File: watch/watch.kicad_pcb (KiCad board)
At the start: 2 copper layers, 36 x 36 mm, 102 parts, among them IC1 IS32FL3237-TQLA3-TR, SW1 ButtonWakeup, U1 STM32L031F4Px, Y1 CR_32kHz

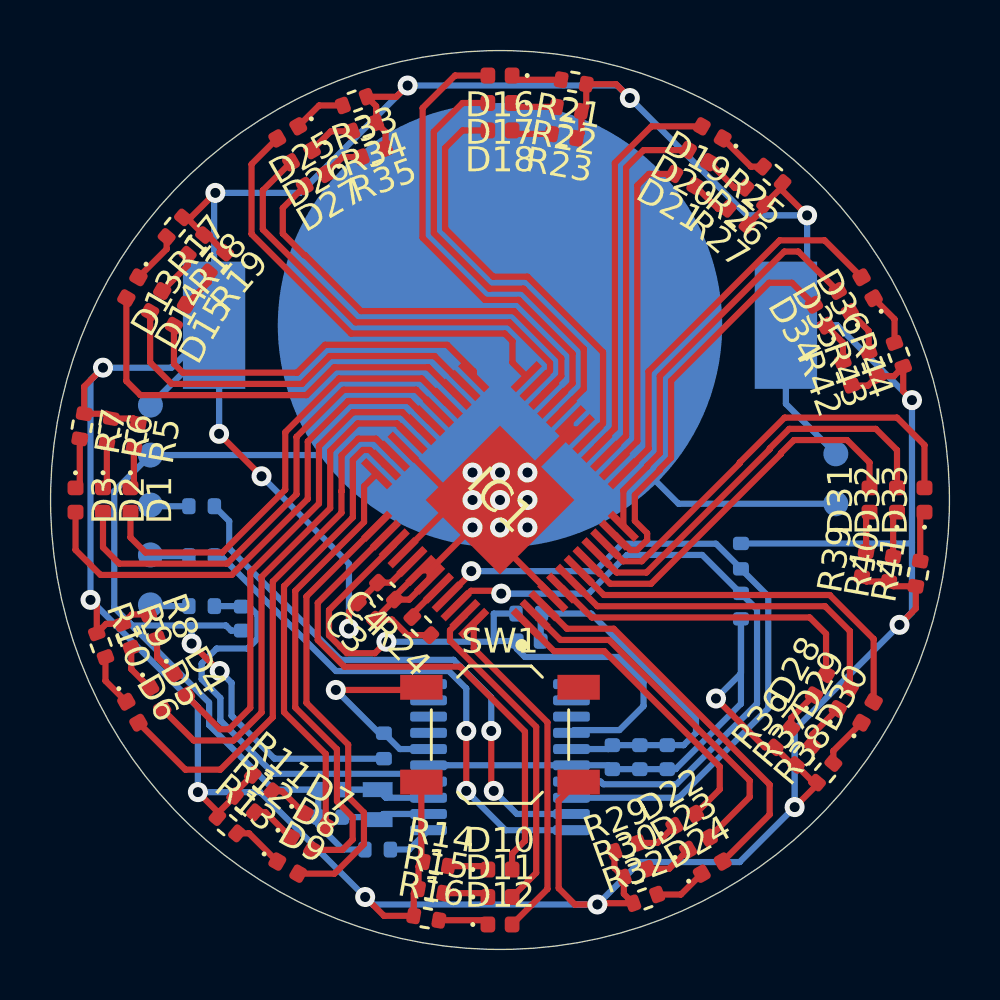
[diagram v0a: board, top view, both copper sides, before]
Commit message: no more vias below metallic components; cleaned up some tracks
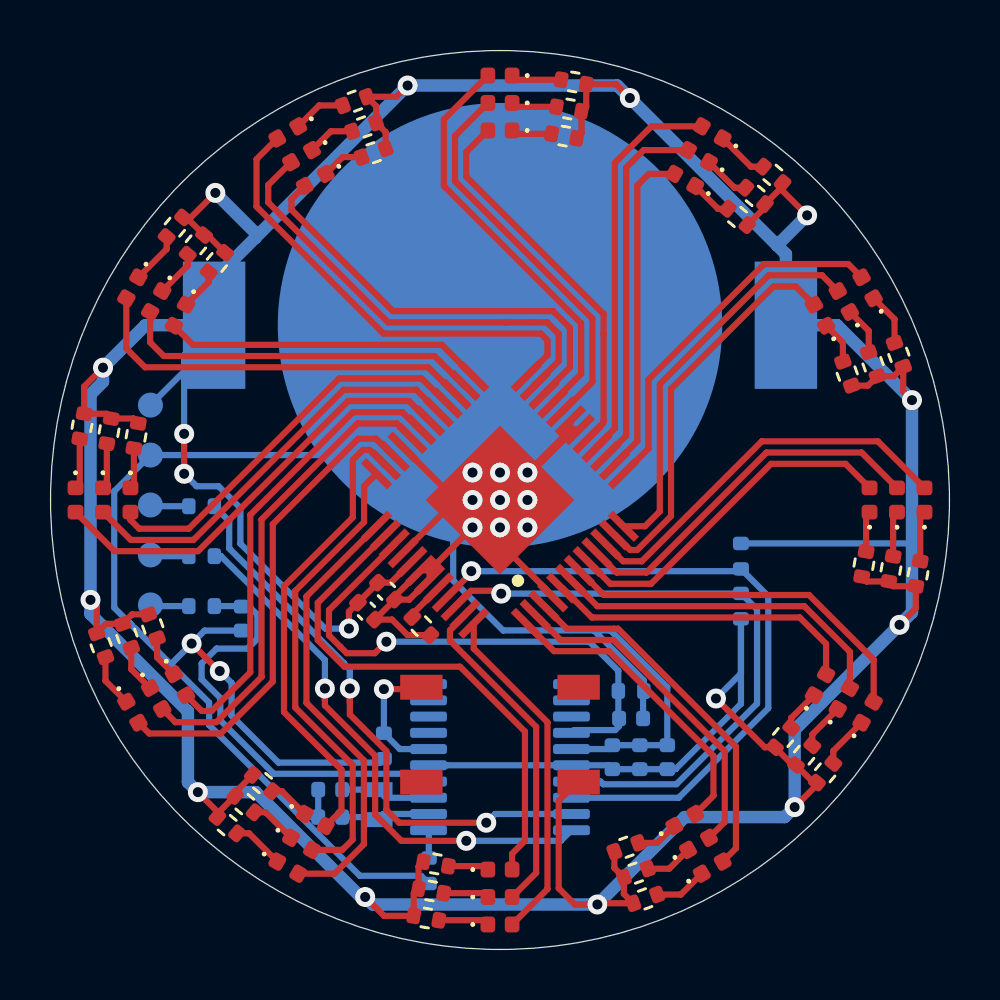
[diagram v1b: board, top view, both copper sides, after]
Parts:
- removed TP6: TP_GND, TestPoint:TestPoint_Pad_D1.0mm
- removed TP7: TP_3V3, TestPoint:TestPoint_Pad_D1.0mm
- moved R20 5.14 mm to (162.5, 113.4)
- moved C2 5.14 mm to (162.5, 114.5)
- moved R4 2.22 mm to (154.4, 120.6), turned to 270 degrees
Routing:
- net +3V3: track 231.2 -> 257.9 mm
- net /LED_Driver/EN: track 25.0 -> 21.6 mm
- net GND: track 125.2 -> 128.2 mm
- net Net-(D3-Pad2): track 20.7 -> 17.6 mm
- net Net-(D2-Pad2): track 19.7 -> 16.8 mm
- net Net-(D1-Pad2): track 18.6 -> 16.0 mm
- net Net-(R51-Pad1): track 8.16 -> 5.69 mm
- net Net-(D18-Pad2): track 17.3 -> 15.2 mm
- net Net-(D6-Pad2): track 21.3 -> 19.3 mm
- net Net-(D16-Pad2): track 18.6 -> 16.6 mm
- net Net-(D15-Pad2): track 14.8 -> 12.9 mm
- net Net-(D33-Pad2): track 17.6 -> 15.8 mm
- net Net-(D17-Pad2): track 17.5 -> 15.7 mm
- net Net-(D32-Pad2): track 16.6 -> 14.9 mm
- net Net-(D13-Pad2): track 17.7 -> 16.0 mm
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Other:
- board text added: "JLCJLCJLCJLC"
- board text added: "V1.0"

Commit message: V2 after Feedback
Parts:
- added TP6: UART_TX, TestPoint:TestPoint_Pad_D1.0mm, B.Cu at (149.2, 108.5)
- added TP7: UART_RX, TestPoint:TestPoint_Pad_D1.0mm, B.Cu at (151.2, 108.5)
- moved C7 8.56 mm to (155.6, 120.6), turned to 90 degrees
- moved C5 0.95 mm to (163.0, 116.0)
- moved R51 0.22 mm to (152.4, 115.5)
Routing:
- net Net-(TP7-Pad1): track 0.00 -> 10.3 mm
- net Net-(TP6-Pad1): track 0.00 -> 9.32 mm
- net GND: track 128.2 -> 137.5 mm, vias 11 -> 5
- net /LED_Driver/EN: track 21.6 -> 30.3 mm
- net +3V3: track 257.9 -> 258.7 mm
